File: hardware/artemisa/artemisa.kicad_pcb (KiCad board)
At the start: 2 copper layers, 151 parts, among them J1 PS2_CONN, J2 MSX_Slot, J3 MSX_Slot, J4 CONN_JOY, J5 CONN_JOY, J6 PWR_conn, J7 Audio_conn, J8 Audio_conn, J9 GFX_Connector_Output, U1 74HC32, U11 74HCT244, U12 74HCT244, U13 74HCT245, U14 74HCT244, U15 74HC74, U16 74HC08, U17 74HC32, U18 Z84C00, U19 82C55A, U2 74HC04, U20 74HC153, U21 74HC139, U22 LM311, U23 74HC138, U24 74HC32, U25 SST39SF0x0, U26 ATMEGA328P, U27 74HC154, U28 74HC595, U29 74HC595, U3 HM62256ALP-10, U30 74HC595, U31 74HC595, U32 74HC595, U33 74HC595, U34 74HC595, U35 74HC595, U36 74HC595, U37 74HC595, U38 4069, U39 74HC07, U4 HM62256ALP-10, U40 74HC74, U41 AY-3-8910, U42 74HC157, U43 74HC157, U44 74HC595, U5 74HCT11, Y1 3.58Mhz, Y2 16Mhz

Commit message: Separate PS2 connector from adjacent ICs
And also add some informational labels to the PCB.
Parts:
- moved J1 1.68 mm to (268.6, 228.4)
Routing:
- net VCC: track 1758.4 -> 1760.8 mm
- net /KBD/KBCOL6: track 242.2 -> 244.1 mm
- net /KBD/KBCOL7: track 248.7 -> 250.6 mm
- net Net-(J1-Pad1): track 48.5 -> 47.4 mm
- net /KBD/KBCOL5: track 236.5 -> 237.5 mm
- net /KBD/KBCOL4: track 234.5 -> 235.6 mm
- net /KBD/KBCOL3: track 230.8 -> 231.8 mm
- net Net-(J1-Pad5): track 42.0 -> 42.6 mm
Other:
- board text added: "CAS IN"
- board text added: "CAS OUT"
- board text added: "JOY A"
- board text added: "JOY B"

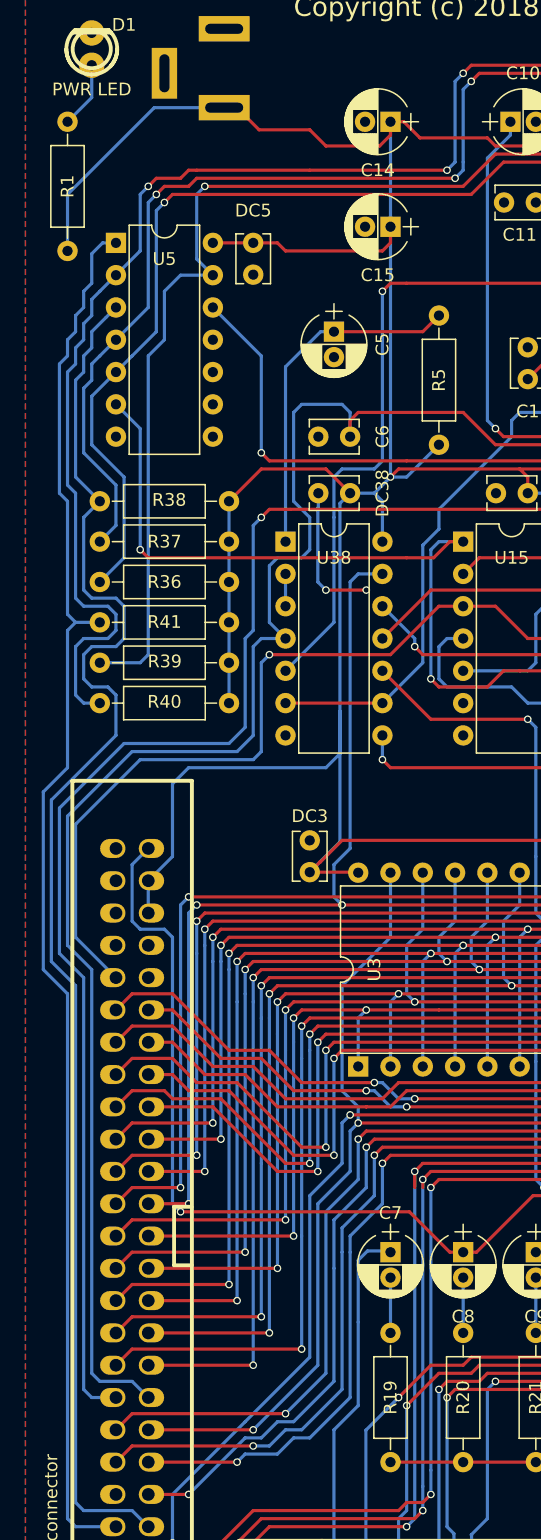
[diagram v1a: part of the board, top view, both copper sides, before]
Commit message: Extract `AUDIO` to GFX output in PCB
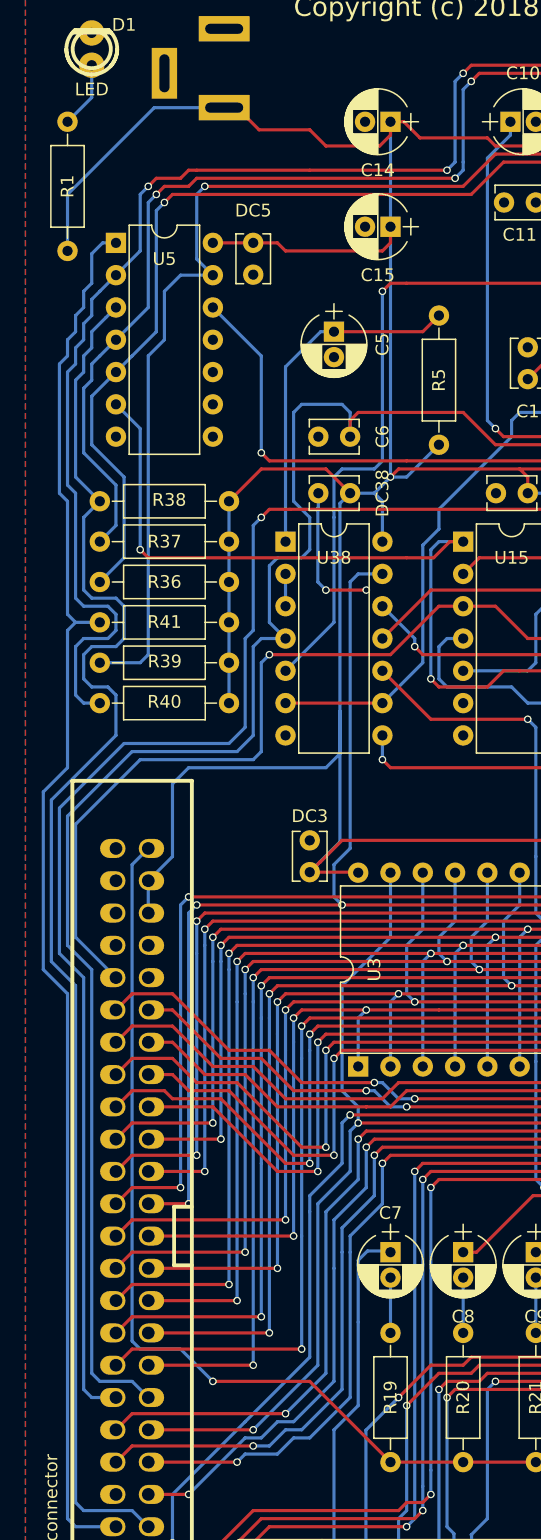
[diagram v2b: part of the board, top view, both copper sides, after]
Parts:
- D1: value PWR LED -> LED
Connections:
- C8 pad 1: /SOUND -> /EXTSOUND
- J2 pad 49: /SOUND -> /EXTSOUND
- J3 pad 49: /SOUND -> /EXTSOUND
- J9 pad 49: /SOUND -> /AUDIO
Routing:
- net /SOUND: track 361.1 -> 0.00 mm, vias 5 -> 0
- net /EXTSOUND: track 0.00 -> 305.7 mm, vias 0 -> 4
- net /AUDIO: track 11.4 -> 75.0 mm, vias 0 -> 1
- net /~CS1: track 288.5 -> 287.2 mm
- net /~CS2: track 309.0 -> 308.4 mm

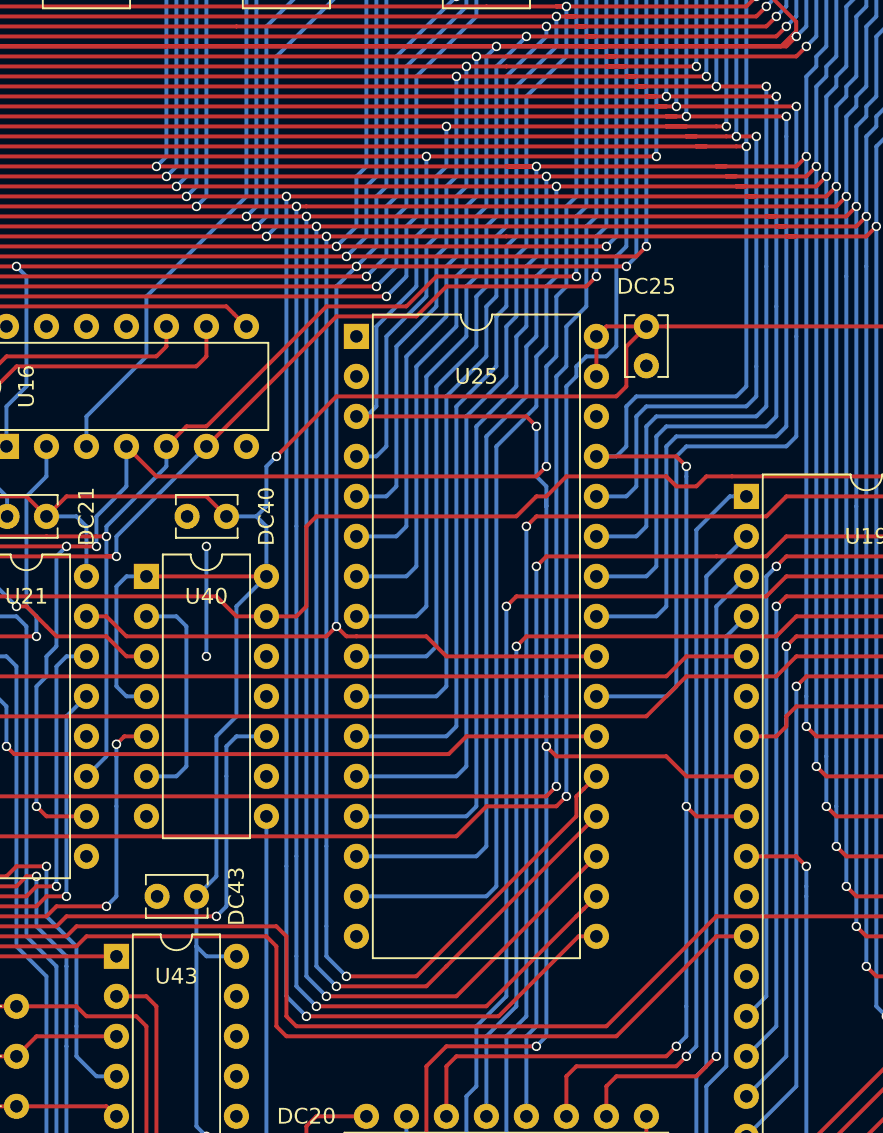
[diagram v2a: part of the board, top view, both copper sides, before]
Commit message: Fix wrong PPI address lines in PCB
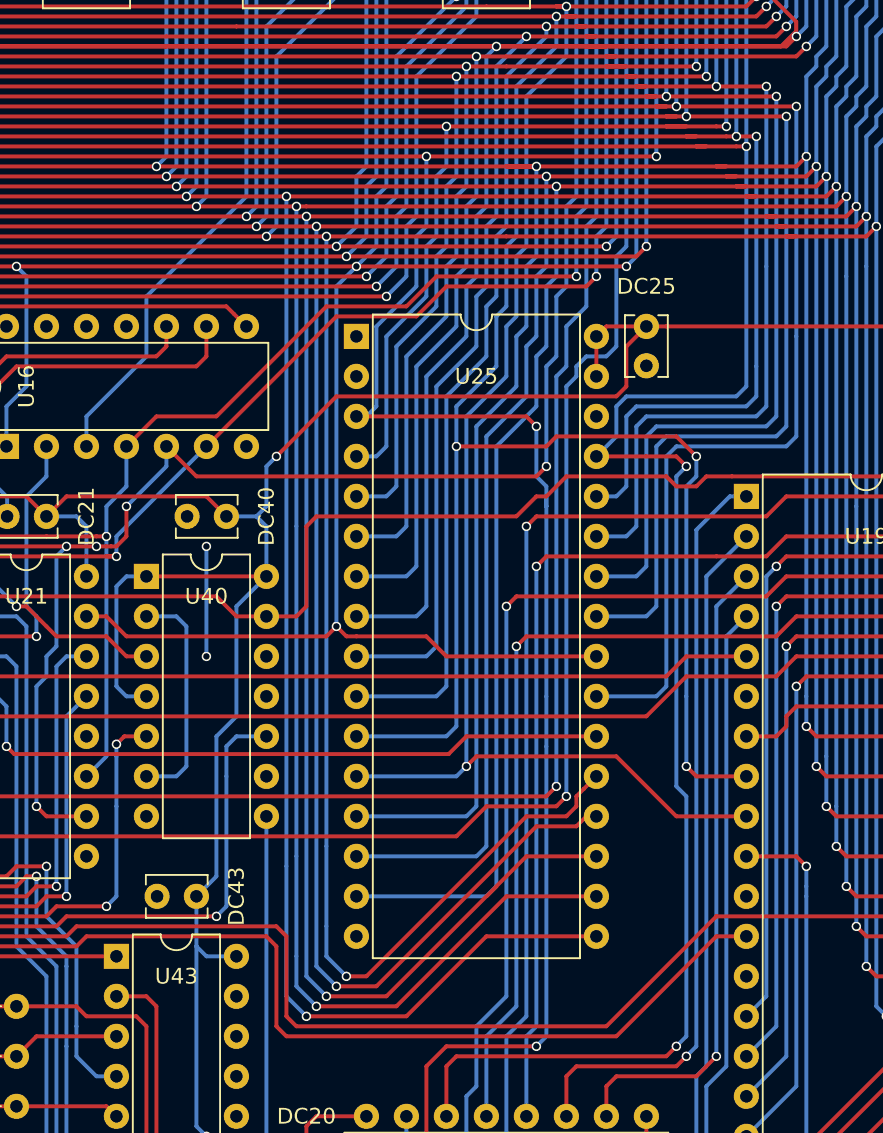
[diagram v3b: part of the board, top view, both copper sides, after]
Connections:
- U16 pad 4: /~CS2 -> /~CS1
- U16 pad 5: /~CS1 -> /~CS2
- U19 pad 8: /ADDR15 -> /ADDR1
- U19 pad 9: /ADDR14 -> /ADDR0
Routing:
- net /ADDR1: track 428.2 -> 468.3 mm, vias 10 -> 13
- net /ADDR0: track 419.9 -> 439.5 mm, vias 9 -> 10
- net /ADDR15: track 536.5 -> 523.0 mm, vias 12 -> 11
- net /ADDR14: track 494.4 -> 490.5 mm, vias 12 -> 11
- net /~CS1: track 287.2 -> 288.7 mm
- net /~CS2: track 308.4 -> 307.6 mm, vias 6 -> 7

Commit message: Move RESET signal general into POWER sheet
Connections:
- net Net-(U19-Pad35) renamed /RESET

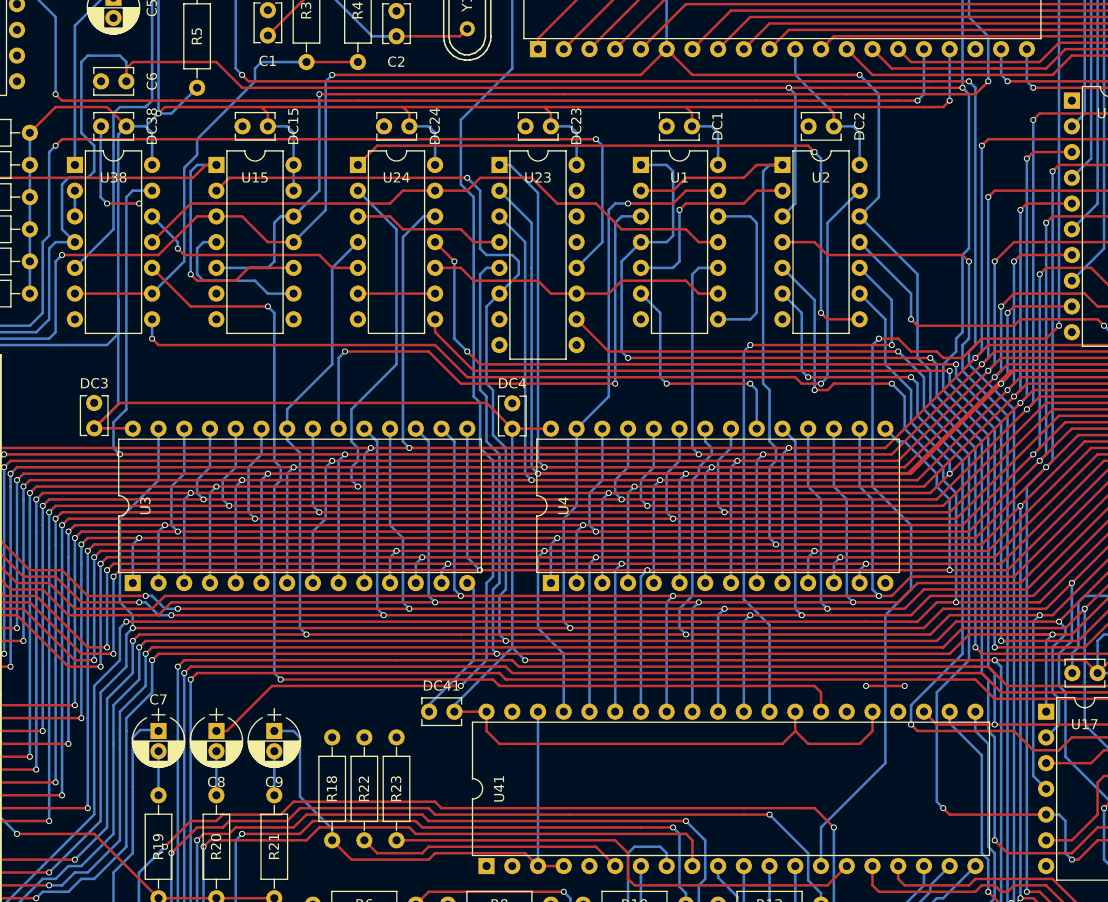
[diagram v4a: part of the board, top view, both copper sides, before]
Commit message: Rearrange the not gates
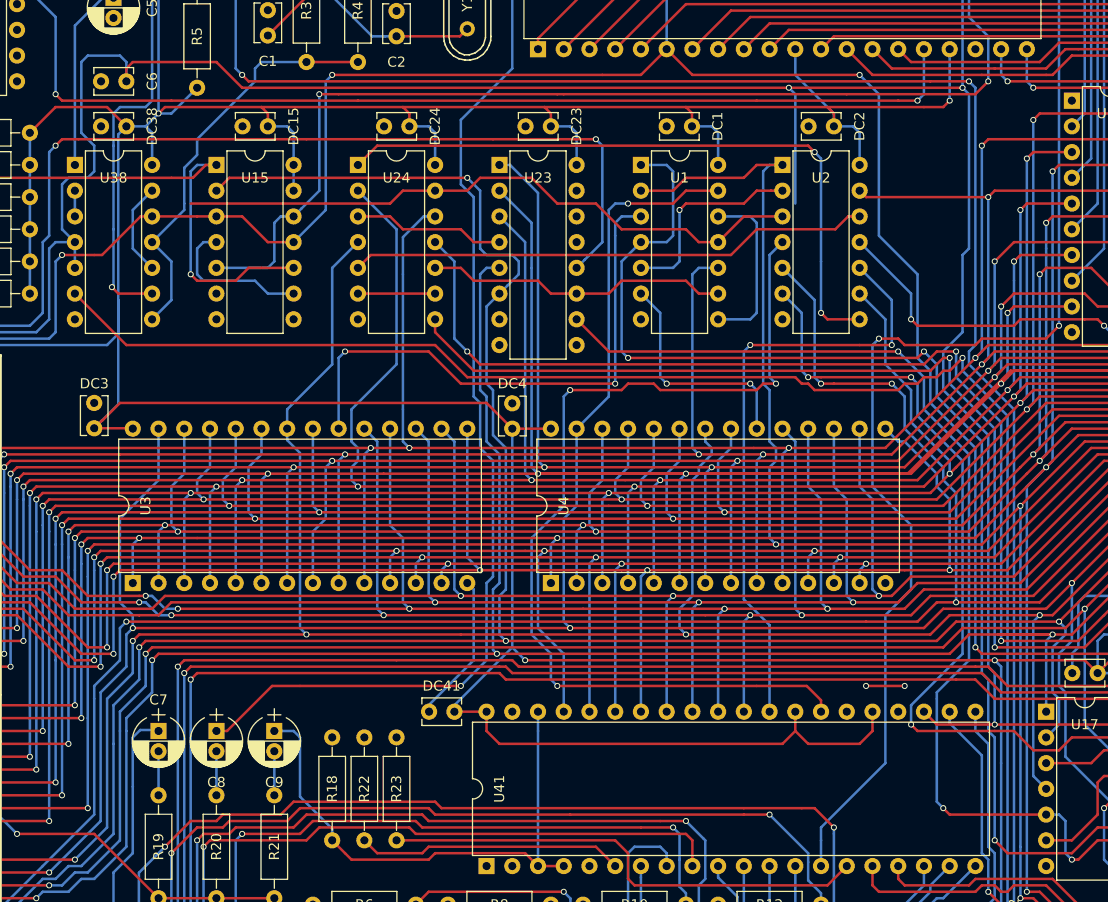
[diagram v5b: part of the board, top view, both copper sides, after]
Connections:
- U2 pad 12: /CLK -> Net-(U2-Pad12)
- U2 pad 13: Net-(U2-Pad13) -> /ADDR1
- U2 pad 3: /~RESET -> Net-(U1-Pad11)
- U2 pad 4: /RESET -> Net-(U2-Pad4)
- U24 pad 5: Net-(U24-Pad5) -> Net-(U2-Pad12)
- U38 pad 11: Net-(U1-Pad11) -> Net-(R3-Pad2)
- U38 pad 12: Net-(U24-Pad5) -> /CLK
- U38 pad 13: /ADDR1 -> Net-(U38-Pad10)
- U38 pad 5: Net-(C2-Pad1) -> /~RESET
- U38 pad 6: Net-(R3-Pad2) -> /RESET
- U38 pad 8: Net-(U2-Pad13) -> Net-(R3-Pad2)
- U38 pad 9: Net-(R3-Pad2) -> Net-(C2-Pad1)
- U41 pad 27: Net-(U38-Pad10) -> Net-(U2-Pad4)
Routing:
- net Net-(U38-Pad10): track 106.7 -> 9.20 mm, vias 2 -> 0
- net Net-(U2-Pad4): track 0.00 -> 95.5 mm, vias 0 -> 3
- net Net-(U2-Pad13): track 90.4 -> 0.00 mm, vias 2 -> 0
- net /RESET: track 188.8 -> 252.7 mm
- net Net-(U2-Pad12): track 0.00 -> 51.6 mm
- net Net-(U24-Pad5): track 22.8 -> 0.00 mm, vias 1 -> 0
- net /ADDR1: track 468.3 -> 452.2 mm, vias 13 -> 12
- net GND: track 159.8 -> 148.7 mm, vias 14 -> 12
- net Net-(C2-Pad1): track 70.0 -> 74.6 mm, vias 1 -> 2
- net Net-(R3-Pad2): track 44.5 -> 41.0 mm
- net Net-(U1-Pad11): track 61.1 -> 63.2 mm
- net Net-(U16-Pad9): track 119.6 -> 121.4 mm
- net Net-(U16-Pad10): track 123.0 -> 124.8 mm, vias 4 -> 3
- net /CLK: track 417.8 -> 416.2 mm
- net /~RFSH: track 347.3 -> 346.0 mm
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
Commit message: Move PSG clock generation into CLOCK sheet
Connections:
- net Net-(U40-Pad5) renamed /PSGCLK

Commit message: Move DATADIR signal generation into DECODING sheet
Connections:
- net Net-(U13-Pad1) renamed /DATADIR
